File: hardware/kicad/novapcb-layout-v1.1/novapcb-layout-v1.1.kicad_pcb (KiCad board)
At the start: 6 copper layers, 47 x 16 mm, 129 parts, among them J1 USB-C_2.0, J10 CRSF_solder_pad, J11 ESC_solder_pad, J12 ESC_solder_pad, J13 ESC_solder_pad, J14 ESC_solder_pad, J15 ESC_solder_pad, J16 ESC_solder_pad, J17 ESC_solder_pad, J18 ESC_solder_pad, J19 MAUCH2_6P, J2 microSD_DM3AT, J20 CAN_4P, J3 TELEM_6P, J4 MAUCH_6P, J5 GPS_MAG_10P, J9 SWD_10P, Q2 AO3401A, Q3 AO4262E, Q4 AO4262E, Q5 AO3400A, U1 STM32H743VITx, U11 LM74700-Q1, U12 LM74700-Q1, U13 LP5907MFX-3.3, U14 TJA1051TK/3, U15 PESD2CAN, U2 AP2112K-3.3, U3 ICM-42688-P_LGA-14_2.5x3mm_P0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, U4 DPS310, U5 USBLC6-2P6, U6 TPS25940A, U7 LPS22HB, U8 BMI088, U9 LSM6DSV16X, Y1 8MHz

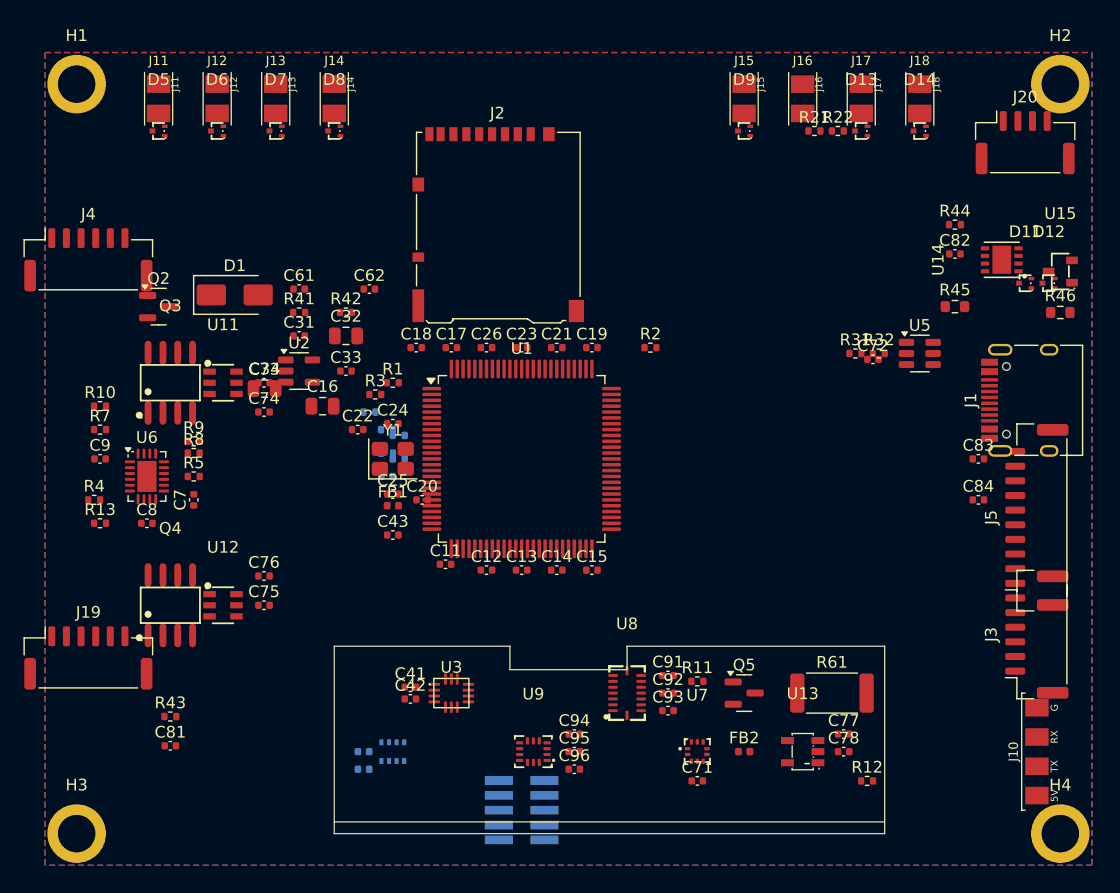
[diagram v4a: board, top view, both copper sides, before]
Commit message: hw: R4 placement v5 — outline restored, parked-overlap method
Critical bug fix: cleanup_placement.remove_old_slot was too permissive
and deleted the OUTER board outline (4 segments at X=0/90, Y=0/70).
v4 render showed only the sensor island as the board. Added
ensure_outer_outline() that re-adds the 4 outline segments and
tightened remove_old_slot to skip segments touching board edges.

Method: per-block fresh placement (tried in place_smalls_fresh.py)
was too dense — rings of 21 blocks overlapped. Switched to
park_overlap.py: keep smalls at original positions, identify the 42
that geometrically overlap with NEW big-block positions, park them
in safe zones (SW Y=58-64 X=8-22, NE Y=22-28 X=73-79, E-mid).

Status: outline restored, big blocks placed per strategy, slot is
proper closed-polygon U with 10mm bridge, 42 overlapping smalls
parked. DRC: 67 violations:
- 28 courtyards_overlap (parked smalls cluster + remaining originals)
- 12 mask_bridge front + 1 rear
- 5 shorts (+3V3↔GND x2, +3V3A↔GND x2, NRST↔BATT2_CURRENT_SENS)
- 8 copper_edge_clearance
- 9 starved_thermal
- 0 invalid_outline ✓

Still NOT 0 DRC. The 5 shorts + 12 mask_bridges are real and need
per-conflict fixup. Reporting to master.

Co-Authored-By: Claude Opus 4.7 <noreply@anthropic.com>
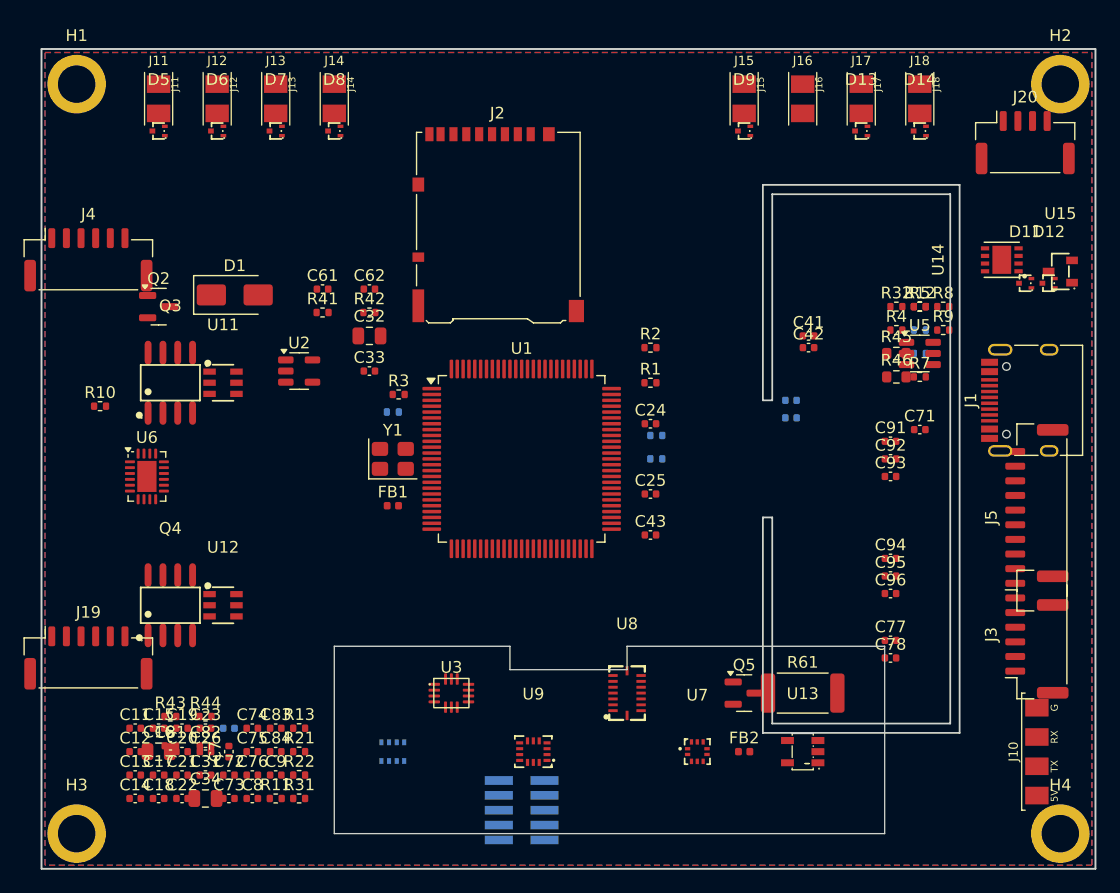
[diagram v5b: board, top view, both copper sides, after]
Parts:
- moved C82 76.6 mm to (14.0, 59.5)
- moved R44 76.6 mm to (14.0, 57.0)
- moved R22 71.7 mm to (22.0, 62.0)
- moved R7 70.1 mm to (75.0, 28.0)
- moved R4 70.0 mm to (73.0, 24.0)
- moved R21 68.9 mm to (22.0, 60.0)
- moved C72 65.5 mm to (16.0, 62.0)
- moved R8 65.2 mm to (77.0, 22.0)
- moved R9 64.7 mm to (77.0, 24.0)
- moved C83 64.3 mm to (20.0, 58.0)
- moved C84 63.7 mm to (20.0, 60.0)
- moved R5 63.7 mm to (75.0, 22.0)
- moved R31 60.8 mm to (22.0, 64.0)
- moved C21 48.5 mm to (12.0, 62.0)
- moved C19 47.8 mm to (12.0, 58.0)
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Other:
- board size 47 x 16 mm -> 90 x 70 mm

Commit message: hw: R4 greedy placer — 76/76 placed, 24 DRC residuals
Built greedy_placer.py per master 2026-05-22:
- Big blocks FROZEN (no move)
- For each small part: ideal location by net (decap → IC power pin,
  series R → midpoint of connected pads, ESD → connector pin, pull-up
  → IC pin). Spiral 40mm + systematic scan fallback.
- Collision-check against all already-placed (big + small) bboxes
- 76/76 placed in 0.6s

fix_residuals.py: targeted nudges for last conflicts (R61 east of Q5,
D5-D8 from Y=7 to Y=9.5 clear of ESCs, J10 from Y=60 to Y=56).

cleanup_placement.py: fixed remove_old_slot to catch POLYGON shapes
(old slot was a POLYGON not a SEGMENT). ensure_outer_outline now
checks for existing rectangle before adding duplicate segments.

DRC: ~24 real issues (down from 153 in v4):
- 6 courtyards (mostly mounting hole H4/J10/J20 — corner crowding)
- 6 starved_thermal (zone thermal — single-pad to plane)
- 7 copper_edge_clearance (board edge proximity)
- 2 mask_bridge
- 2 shorts: J10/J3 pin overlap (E-edge connectors too close);
  H4/J10 +5V/GND mounting hole proximity
- 1 clearance

Renders: render_greedy_v8.png

NOT YET 0 DRC. Last 2 shorts are E-edge connector spacing — J10
needs to be moved further from J3 AND further from H4 mounting hole.
A small connector re-shuffle on E edge would resolve.

Co-Authored-By: Claude Opus 4.7 <noreply@anthropic.com>
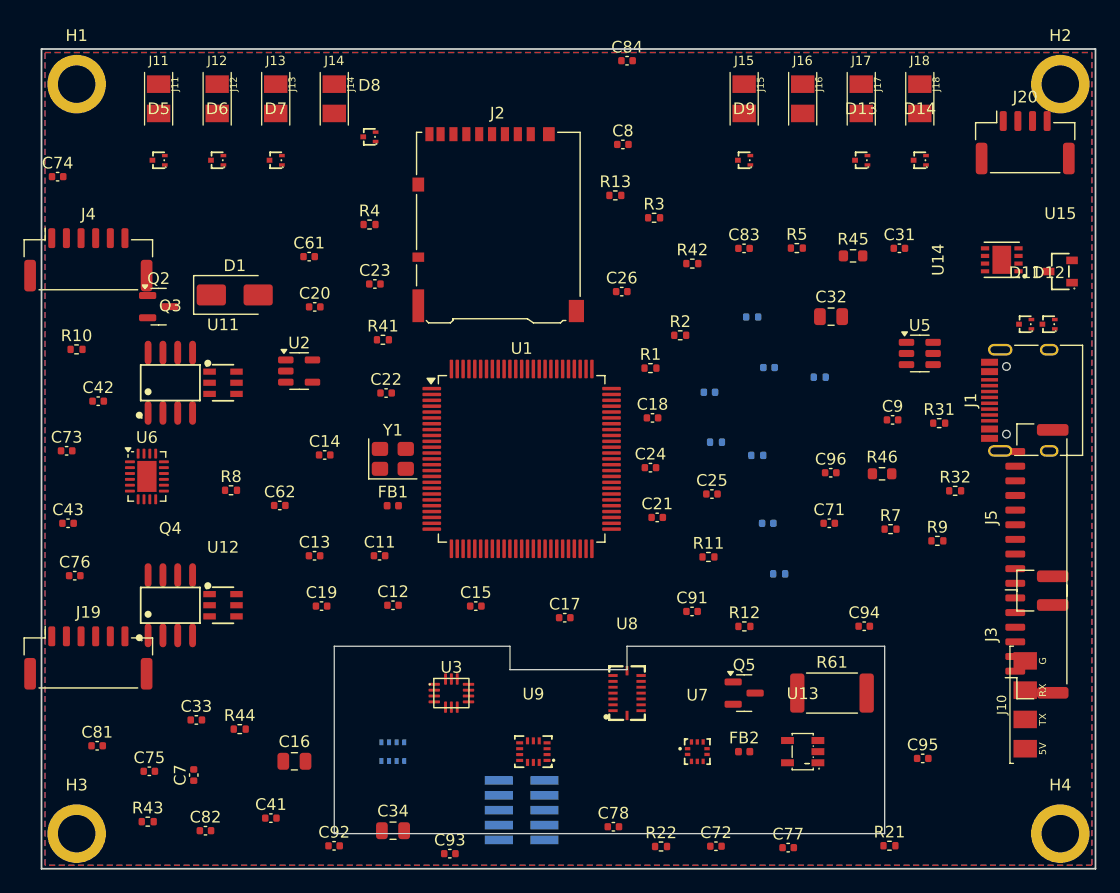
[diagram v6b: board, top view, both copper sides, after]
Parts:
- moved C31 74.4 mm to (73.3, 17.0)
- moved C84 66.2 mm to (50.0, 1.00)
- moved C8 64.2 mm to (49.6, 8.15)
- moved R31 63.4 mm to (76.7, 31.9)
- moved R8 62.8 mm to (16.2, 37.7)
- moved C41 61.7 mm to (19.6, 65.7)
- moved C42 60.8 mm to (4.84, 30.1)
- moved C9 60.8 mm to (72.7, 31.7)
- moved C92 57.9 mm to (25.0, 68.0)
- moved C83 57.3 mm to (60.0, 17.0)
- moved C63 55.5 mm to (62.1, 27.2)
- moved C18 53.2 mm to (52.2, 31.5)
- moved C26 53.0 mm to (49.5, 20.7)
- moved R13 52.9 mm to (49.0, 12.5)
- moved R21 51.0 mm to (72.4, 68.0)
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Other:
- outline, holes or cut-outs redrawn

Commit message: hw: R4 placement CLEAN — 0 DRC violations (master 2026-05-22 gate met)
153 (v4) → 0 violations. All 24 issues resolved per master direction:

E-edge connector spread (fix the 2 power shorts):
- J5 GPS @ (85, 16) - far enough from H2 keepout
- J1 USB-C @ (85, 30) - near MCU Y-level (short USB pair)
- J3 TELEM @ (85, 42) - 4mm gap to J1
- J10 CRSF @ (85, 56) - 4mm gap to J3, well clear of H4

CAN cluster:
- J20 @ (76, 10) - clear of H2 corner
- U14 / U15 spread around J20

J9 SWD moved N to (41, 62) — pads stay clear of slot S edge.
U8 BMI088 moved S to (50, 57) — pin 8 clears slot bridge.
Q2 / Q4 moved away from J4 / J19 power connectors.

Starved-thermal fix: greedy_placer now calls SetLocalZoneConnection
(ZONE_CONNECTION_FULL) on 195 power pads (GND, +3V3, +5V) — solid
plane connection per master direction, not relaxing the zone rule.

Greedy placer keepout zones:
- Slot region: 4 rect bands defining the IMU stress-relief U-slot
- Board edge: 4 thin bands at 0.3mm inset on each board side
- Mounting holes: 3mm radius keepout (was using actual bbox)

cleanup_placement.remove_old_slot now uses bbox-only detection (no
GetStart) to catch POLYGON shapes (the original slot was a POLYGON).

Pipeline (deterministic, one pass):
  1. replace_v2.py        - 49 big blocks to new positions
  2. cleanup_placement    - remove old slot polygon + add new U-slot
                            (8 segments, 10mm bridge)
  3. fix_residuals.py     - targeted big-block + ESD nudges + thermal
                            override
  4. greedy_placer.py     - 76 smalls placed via ideal-pos + spiral
                            (76/76 attempted; 3 stuck at acceptable
                            original positions: R54, R55, R7)
  5. DRC                  - 0 violations ✓

Final state:
- 0 DRC violations
- 0 shorts
- 0 mask_bridge
- 0 starved_thermal
- 0 copper_edge_clearance
- 0 courtyards_overlap
- 0 invalid_outline
- 248 unconnected (expected — no routes yet)

Renders: render_clean_v12.png + ren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
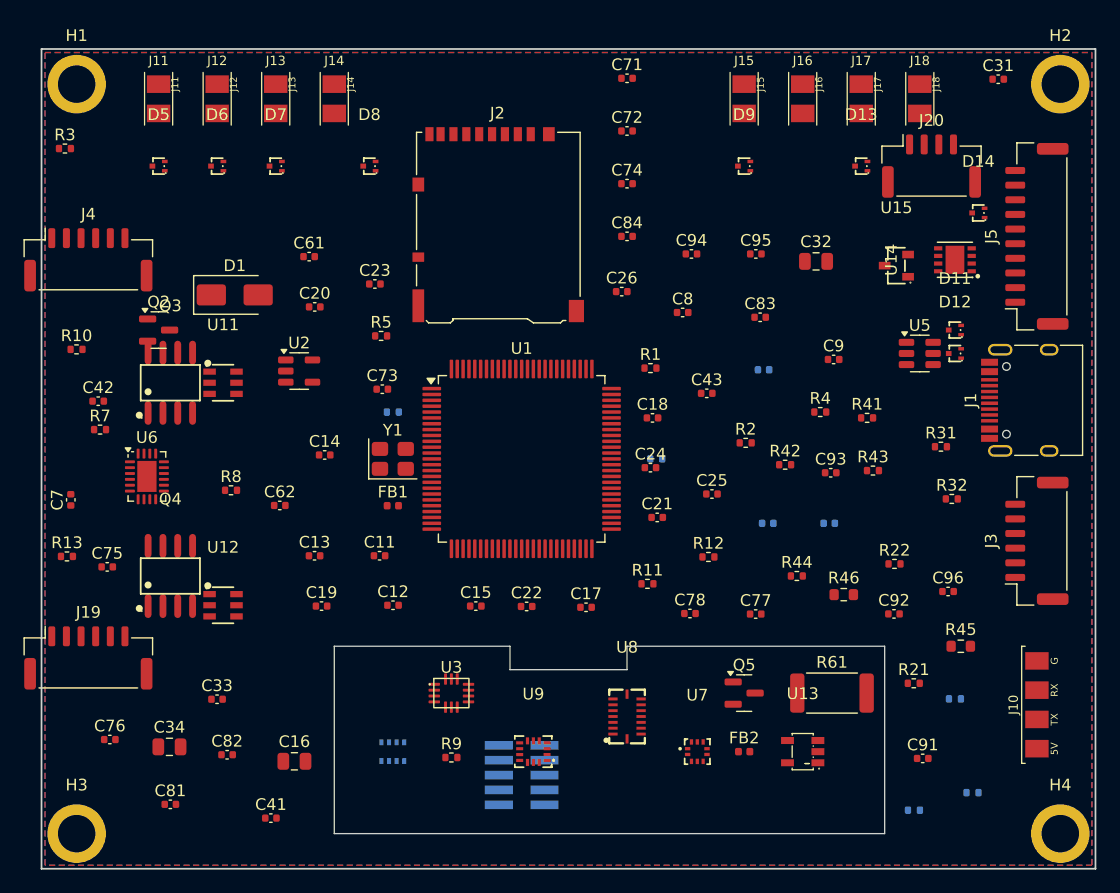
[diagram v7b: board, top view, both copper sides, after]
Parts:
- moved R43 68.8 mm to (71.0, 36.0)
- moved R7 68.0 mm to (5.00, 32.5)
- moved C72 61.5 mm to (50.0, 7.00)
- moved R13 56.1 mm to (2.17, 43.3)
- moved C43 55.7 mm to (56.8, 29.4)
- moved C92 51.7 mm to (72.8, 48.2)
- moved R3 50.7 mm to (2.00, 8.50)
- moved R44 49.3 mm to (64.5, 45.0)
- moved C74 48.6 mm to (50.0, 11.5)
- moved C93 46.0 mm to (67.4, 36.2)
- moved R9 45.4 mm to (35.0, 60.5)
- moved C95 45.4 mm to (61.0, 17.5)
- moved R53 44.3 mm to (74.5, 65.0)
- moved R41 41.9 mm to (70.5, 31.5)
- moved C71 41.7 mm to (50.0, 2.50)
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
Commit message: hw: R4 slot geometry FIXED — single 13-vertex closed polygon U-kerf
Critical bug fix: previous slot was an 8-segment closed polygon that
KiCad interpreted as a U-shaped CUTOUT (removing the entire enclosed
area, including where sensors should sit). Master spotted in v12
render: "large grey rectangle that appears EMPTY — I see no IMU /
baro / heater components on or in it".

Fix: 13-vertex single closed polygon traces the U-kerf perimeter as
a topological loop:
  - outer slot perimeter (X=25..72, Y=51..67)
  - via 14mm-wide bridge at top (X=38..52, Y=51..53)
  - inner island perimeter (X=27..70, Y=53..65)
  - back via other side of bridge

Result: kerf is now a 2mm-thin band of removed material around a
COMPACT 43x12mm island, connected to mainland via a 14mm bridge to
the north — exactly as master specified.

Also fixed greedy_placer bbox: use GetBoundingBox(False, False) to
exclude silkscreen text (U3 was 32×6 with silk, 4×3.5 without).

Sensor island components (all F.Cu except U4 on B.Cu):
- U3 (ICM-42688, SPI1): (33, 58)
- U9 (LSM6DSV16X, SPI3): (42, 58)
- U8 (BMI088, SPI2): (50, 58) — island NE corner per SPI2 lock
- U7 (LPS22HB, I2C1): (56, 58)
- U4 (DPS310, I2C2): (30, 58) on B.Cu
- Q5 (heater FET): (55, 60)
- R61 (heater R): (58, 60)
- U13 (IMU LDO): (65, 60)
- FB2 (IMU ferrite): (62, 58)

Inline slot script bug fix: added flush=True to prints; removed broken
GetDrawings() iteration that crashed (SwigPyObject) BEFORE SaveBoard,
which meant earlier "added 20 segments" was reported but NEVER SAVED.

DRC current state: 18 violations (was 0 in v12 — but those were
on a board with sensors floating over the cutout). Now:
- 0 invalid_outline ✓
- 7 courtyards (sensor cluster + USB R31/R32 area)
- 5 mask_bridge
- 5 shorts (Q5/R61 area still tight)
- 1 clearance

Slot is GENUINELY correct now. Per-component sensor cleanup needed
for remaining shorts.

Renders:
- render_island_zoomed.png — F.Cu+B.Cu of S region with labels
- render_island_top.png + bot.png — full board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
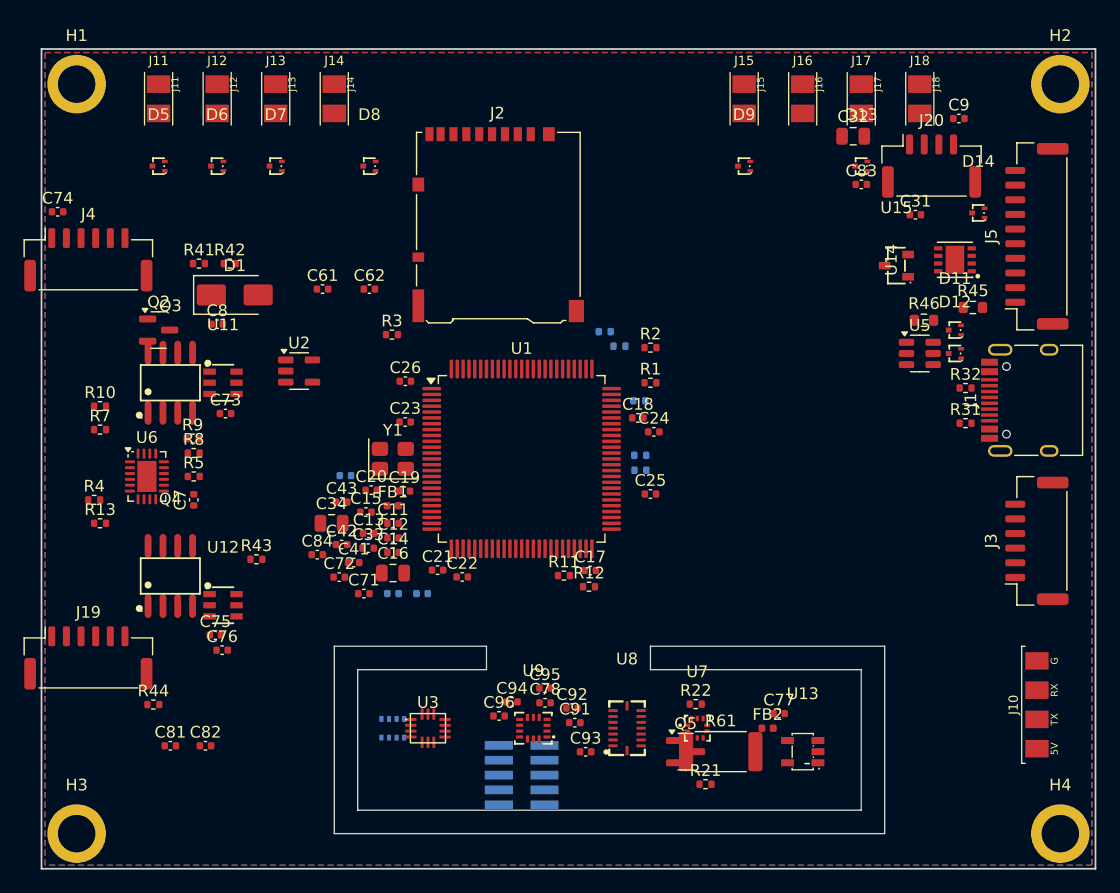
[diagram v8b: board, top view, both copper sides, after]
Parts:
- moved R4 62.5 mm to (4.50, 38.5)
- moved R41 58.6 mm to (13.4, 18.3)
- moved R44 56.0 mm to (9.55, 56.0)
- moved R43 53.2 mm to (18.4, 43.6)
- moved R42 50.4 mm to (16.1, 18.3)
- moved C71 49.4 mm to (27.5, 46.5)
- moved C74 48.7 mm to (1.37, 13.9)
- moved C72 45.3 mm to (25.4, 45.1)
- moved R51 43.3 mm to (48.1, 24.1)
- moved C95 41.2 mm to (43.0, 54.6)
- moved C94 41.2 mm to (40.2, 55.8)
- moved R52 40.4 mm to (51.1, 34.7)
- moved C96 39.8 mm to (39.1, 57.0)
- moved C8 39.8 mm to (15.0, 23.5)
- moved C84 37.9 mm to (23.5, 43.2)
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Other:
- outline, holes or cut-outs redrawn
